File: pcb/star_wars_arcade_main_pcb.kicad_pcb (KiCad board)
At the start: 2 copper layers, 292.1 x 525.8 mm, 322 parts, among them J16 Aud_Conn, J17 Main_Connector, J18 Cat_Box_Conn, J20 J20, Q1 2N3904, Q3 Q_NPN_BCE, Q4 Q_NPN_BCE, SW1 L_11, SW2 D_10, SW3 E/F_10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

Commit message: 661 unconnected signal remain
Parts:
- moved R95 0.64 mm to (65.4, 203.8)
- moved R97 0.64 mm to (69.2, 201.3)
- moved CR2 0.63 mm to (54.6, 170.2)
- moved R91 0.63 mm to (54.0, 154.9)
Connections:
- D_9 pad 12: 3GCLK -> 1.5GCLK
- D_9 pad 13: 1.5GCLK -> 3GCLK
- K_9 pad 14: D6 -> D1
- K_9 pad 15: D5 -> D2
- K_9 pad 17: D7 -> D0
- K_9 pad 18: D3 -> D4
- K_9 pad 19: D2 -> D5
- K_9 pad 20: D1 -> D6
- K_9 pad 21: D0 -> D7
- K_9 pad 8: D4 -> D3
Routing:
- net D1: track 284.5 -> 626.1 mm
- net D2: track 309.2 -> 630.6 mm, vias 6 -> 8
- net ~PRNGCLR: track 57.8 -> 366.0 mm, vias 0 -> 2
- net GND: track 7544.9 -> 7828.7 mm, vias 59 -> 60
- net Net-(C_10-Pad10): track 48.9 -> 229.2 mm, vias 1 -> 4
- net ~OPT0: track 0.00 -> 168.3 mm, vias 0 -> 2
- net D7: track 575.2 -> 729.5 mm
- net Net-(D_8-Pad1): track 7.62 -> 159.4 mm, vias 1 -> 2
- net ~OPT1: track 0.00 -> 144.8 mm, vias 0 -> 2
- net AB0: track 523.2 -> 662.3 mm
- net 750KHZ: track 174.6 -> 301.6 mm, vias 1 -> 2
- net ~IN1: track 0.00 -> 126.4 mm, vias 0 -> 2
- net ~RECALL: track 103.5 -> 224.8 mm
- net AB1: track 567.1 -> 687.7 mm, vias 5 -> 6
- net ~RESET: track 380.2 -> 497.1 mm, vias 5 -> 6
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
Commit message: 557 unconnected signals remain
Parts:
- moved R94 1.27 mm to (127.6, 203.2)
- moved C21 0.64 mm to (39.4, 267.3)
- moved C74 0.64 mm to (39.4, 230.5)
- moved C75 0.63 mm to (108.6, 243.2)
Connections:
- N_8 pad 1: 3MHZ -> ~R~WB
- N_8 pad 2: ~R~WB -> 3MHZ
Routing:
- net ~R~WB: track 0.00 -> 470.8 mm, vias 0 -> 3
- net 12MHZ: track 228.0 -> 595.0 mm, vias 4 -> 5
- net AB7: track 346.1 -> 652.8 mm, vias 2 -> 3
- net Net-(N_8-Pad6): track 10.2 -> 275.6 mm, vias 0 -> 2
- net ~OUTS: track 0.00 -> 250.2 mm, vias 0 -> 1
- net 3MHZ: track 260.4 -> 508.5 mm, vias 2 -> 3
- net ~WE: track 294.0 -> 542.2 mm, vias 3 -> 5
- net ~IRQCLR: track 0.00 -> 235.6 mm
- net ~REN: track 0.00 -> 230.8 mm, vias 0 -> 3
- net Net-(K_2-Pad5): track 17.8 -> 247.3 mm, vias 1 -> 2
- net ~MW0: track 0.00 -> 226.7 mm, vias 0 -> 3
- net DS1: track 0.00 -> 222.2 mm, vias 0 -> 4
- net ~3MHZ*: track 16.1 -> 235.8 mm, vias 1 -> 5
- net P93: track 77.5 -> 286.4 mm, vias 1 -> 5
- net ~MBCON: track 174.6 -> 348.2 mm, vias 1 -> 3
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
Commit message: Added more signal traces
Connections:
- M_6 pad 1: Net-(L_6-Pad6) -> Net-(L_6-Pad3)
- M_6 pad 3: Net-(L_6-Pad3) -> Net-(M_6-Pad3)
- N_6 pad 10: Net-(N_6-Pad10) -> Net-(L_6-Pad6)
- P_6 pad 14: Net-(N_6-Pad10) -> Net-(M_6-Pad3)
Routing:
- net Net-(E_6-Pad11): track 15.5 -> 221.5 mm, vias 1 -> 2
- net ~RESET: track 497.1 -> 696.7 mm, vias 6 -> 8
- net ~6MHZ: track 36.8 -> 210.2 mm
- net Net-(M_7-Pad8): track 0.00 -> 167.8 mm, vias 0 -> 3
- net IP1: track 17.8 -> 173.4 mm, vias 1 -> 2
- net ~MW2: track 0.00 -> 144.1 mm, vias 0 -> 1
- net 3MHZ*: track 161.8 -> 293.5 mm, vias 4 -> 6
- net MDB3: track 61.0 -> 177.2 mm, vias 1 -> 4
- net DD2: track 0.00 -> 112.7 mm, vias 0 -> 2
- net MDB4: track 54.2 -> 153.3 mm, vias 1 -> 3
- net DD7: track 0.00 -> 99.1 mm, vias 0 -> 2
- net MDB5: track 38.1 -> 130.2 mm, vias 0 -> 2
- net MDB0: track 54.6 -> 137.7 mm, vias 0 -> 3
- net DB6: track 21.6 -> 101.0 mm, vias 1 -> 3
- net IP7: track 22.9 -> 96.5 mm
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
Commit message: 241 unconnected signals remain
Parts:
- moved C75 0.64 mm to (108.6, 242.6)
- moved C52 0.64 mm to (39.4, 464.2)
- moved C56 0.64 mm to (39.4, 424.2)
- moved C66 0.64 mm to (39.4, 305.4)
- moved C59 0.63 mm to (40.0, 384.2)
- moved C64 0.63 mm to (189.2, 359.4)
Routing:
- net ~EVMEM: track 149.5 -> 484.6 mm, vias 3 -> 5
- net R~W~B: track 371.7 -> 680.3 mm, vias 5 -> 6
- net ~MBRAM: track 76.5 -> 362.8 mm, vias 2 -> 4
- net DB3: track 70.1 -> 339.5 mm, vias 1 -> 6
- net ~DVSRH: track 139.6 -> 368.5 mm, vias 3 -> 5
- net DB6: track 101.0 -> 329.0 mm, vias 3 -> 6
- net AB0: track 662.3 -> 887.1 mm, vias 9 -> 12
- net ~ENA: track 18.4 -> 239.8 mm, vias 1 -> 3
- net DB5: track 73.0 -> 293.4 mm, vias 1 -> 4
- net Net-(E_6-Pad5): track 12.1 -> 228.2 mm, vias 1 -> 2
- net DB4: track 50.2 -> 259.7 mm, vias 1 -> 3
- net Net-(E_5-Pad2): track 19.0 -> 228.6 mm, vias 1 -> 2
- net ~ENB: track 45.7 -> 251.5 mm, vias 1 -> 2
- net DB7: track 167.0 -> 368.3 mm, vias 2 -> 4
- net DB0: track 127.0 -> 300.0 mm, vias 1 -> 2
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
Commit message: 63 disconnected signals remain
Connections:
- D_4 pad 13: D6 -> DB6
- D_4 pad 14: D4 -> DB4
- D_4 pad 15: D2 -> DB2
- D_4 pad 16: D0 -> DB0
- D_4 pad 4: D1 -> DB1
- D_4 pad 5: D3 -> DB3
- D_4 pad 6: D5 -> DB5
- D_4 pad 7: D7 -> DB7
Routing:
- net 1.5MHZ: track 314.9 -> 628.6 mm, vias 5 -> 8
- net DB7: track 368.3 -> 664.7 mm, vias 4 -> 6
- net DB1: track 160.7 -> 434.9 mm, vias 1 -> 5
- net ~R~WB: track 470.8 -> 714.3 mm, vias 3 -> 5
- net R~W: track 83.8 -> 321.9 mm, vias 1 -> 3
- net ECLKQ: track 139.1 -> 366.7 mm, vias 3 -> 5
- net A15: track 156.8 -> 362.8 mm, vias 0 -> 2
- net P96: track 84.5 -> 273.1 mm
- net Net-(M_3-Pad10): track 0.00 -> 177.8 mm, vias 0 -> 1
- net DB6: track 329.0 -> 501.7 mm, vias 6 -> 7
- net 3MHZ: track 531.4 -> 700.3 mm
- net DB0: track 300.0 -> 467.6 mm
- net DD13: track 31.7 -> 198.0 mm, vias 1 -> 3
- net AB0: track 887.1 -> 1048.6 mm, vias 12 -> 13
- net DB4: track 259.7 -> 419.7 mm, vias 3 -> 5
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
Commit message: Completed the layout!
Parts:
- added R1000: 180, Star_Wars_Vector_PCB:GenericComp, F.Cu at (251.5, 138.4)
- moved TP3MHZ1 0.64 mm to (88.9, 462.9)
- moved TPROM4 0.63 mm to (102.2, 463.6)
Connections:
- J_3 pad 12: Net-(J_3-Pad12) -> P96
- K_3 pad 12: Net-(K_3-Pad12) -> P96
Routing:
- net AB9: track 289.6 -> 502.2 mm, vias 5 -> 6
- net ~ROM4: track 57.8 -> 264.2 mm
- net ~ROM3: track 52.7 -> 252.7 mm, vias 0 -> 1
- net 6MHZ: track 155.2 -> 334.9 mm
- net ~ROM2: track 68.6 -> 233.0 mm, vias 0 -> 1
- net AB10: track 301.6 -> 462.9 mm
- net ~ROM0: track 151.8 -> 306.1 mm, vias 1 -> 3
- net ~NOVRAM: track 0.00 -> 144.1 mm, vias 0 -> 2
- net ~NSTORE: track 196.2 -> 307.6 mm, vias 1 -> 2
- net BIC1: track 0.00 -> 92.7 mm
- net ~EVMEM: track 608.5 -> 699.3 mm
- net Net-(B/C_0-Pad13): track 109.7 -> 198.0 mm
- net AB8: track 362.6 -> 448.9 mm
- net BIC2: track 8.26 -> 83.2 mm
- net BIC0: track 0.00 -> 69.2 mm
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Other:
- board text added: "Designed By Nick Mikstas"

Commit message: Updated readme file
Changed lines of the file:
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@@
     (thickness 1.6)
     (drawings 118)
-    (tracks 10588)
+    (tracks 10589)
     (zones 0)
     (modules 323)
@@
     (visible_elements 7FFFF7FF)
     (pcbplotparams
-      (layerselection 0x010fc_ffffffff)
+      (layerselection 0x010f0_ffffffff)
       (usegerberextensions false)
       (usegerberattributes false)
@@
   (segment (start 122.555 363.22) (end 124.46 363.22) (width 0.381) (layer B.Cu) (net 123))
   (segment (start 124.46 363.22) (end 124.46 359.41) (width 0.381) (layer B.Cu) (net 123))
-  (segment (start 122.555 323.215) (end 123.825 323.215) (width 0.381) (layer B.Cu) (net 123))
-  (segment (start 123.825 323.215) (end 123.825 332.74) (width 0.381) (layer B.Cu) (net 123))
-  (segment (start 123.825 332.74) (end 124.46 332.74) (width 0.381) (layer B.Cu) (net 123))
-  (segment (start 124.46 332.74) (end 124.46 340.995) (width 0.381) (layer B.Cu) (net 123))
-  (segment (start 124.46 340.995) (end 123.825 340.995) (width 0.381) (layer B.Cu) (net 123))
-  (segment (start 123.19 342.265) (end 123.825 342.265) (width 0.381) (layer B.Cu) (net 123))
-  (segment (start 123.825 340.995) (end 123.825 342.265) (width 0.381) (layer B.Cu) (net 123))
-  (segment (start 123.825 342.265) (end 123.825 344.805) (width 0.381) (layer B.Cu) (net 123))
-  (segment (start 124.46 344.805) (end 124.46 359.41) (width 0.381) (layer B.Cu) (net 123))
-  (segment (start 123.825 344.805) (end 124.46 344.805) (width 0.381) (layer B.Cu) (net 123))
   (segment (start 161.29 274.955) (end 163.83 274.955) (width 0.381) (layer B.Cu) (net 123))
   (segment (start 161.29 309.245) (end 161.29 274.955) (width 0.381) (layer B.Cu) (net 123))
@@
   (segment (start 247.015 361.95) (end 247.015 360.68) (width 0.381) (layer F.Cu) (net 123))
   (segment (start 222.885 363.22) (end 222.885 361.95) (width 0.381) (layer F.Cu) (net 123))
+  (segment (start 123.825 344.805) (end 124.46 344.805) (width 0.381) (layer B.Cu) (net 123))
+  (segment (start 123.825 323.215) (end 123.825 332.74) (width 0.381) (layer B.Cu) (net 123))
+  (segment (start 124.46 332.74) (end 124.46 340.995) (width 0.381) (layer B.Cu) (net 123))
+  (segment (start 123.825 332.74) (end 124.46 332.74) (width 0.381) (layer B.Cu) (net 123))
+  (segment (start 124.46 344.805) (end 124.46 359.41) (width 0.381) (layer B.Cu) (net 123))
+  (segment (start 122.555 323.215) (end 123.825 323.215) (width 0.381) (layer B.Cu) (net 123))
+  (segment (start 124.46 340.995) (end 123.825 340.995) (width 0.381) (layer B.Cu) (net 123))
+  (segment (start 123.825 344.805) (end 123.825 342.9) (width 0.381) (layer B.Cu) (net 123))
+  (segment (start 123.825 342.9) (end 123.19 342.265) (width 0.381) (layer B.Cu) (net 123))
+  (segment (start 123.825 340.995) (end 123.825 341.63) (width 0.381) (layer B.Cu) (net 123))
+  (segment (start 123.825 341.63) (end 123.19 342.265) (width 0.381) (layer B.Cu) (net 123))
   (segment (start 241.935 355.6) (end 229.87 355.6) (width 0.381) (layer F.Cu) (net 124))
   (segment (start 229.87 355.6) (end 229.87 355.6) (width 0.381) (layer F.Cu) (net 124))

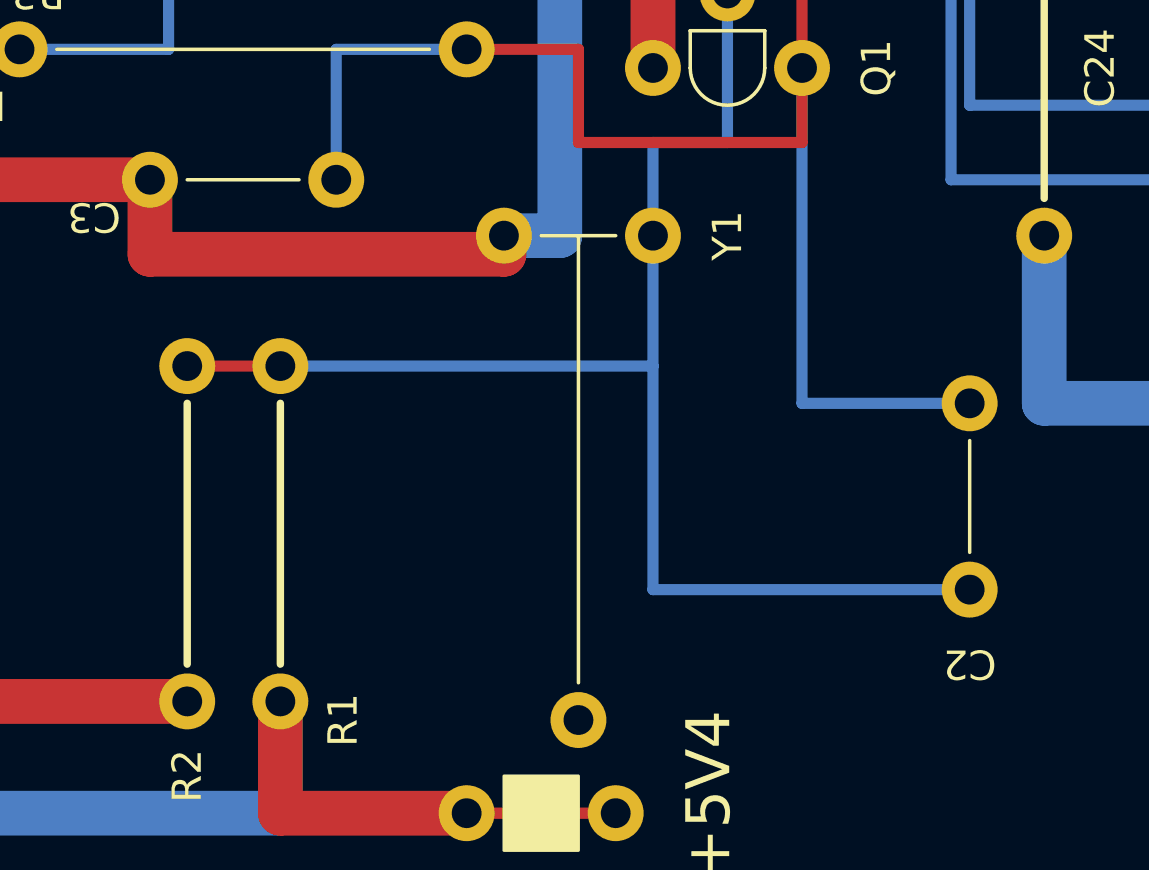
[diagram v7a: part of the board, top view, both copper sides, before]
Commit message: Added BOM and fixed minor silkscreen issues
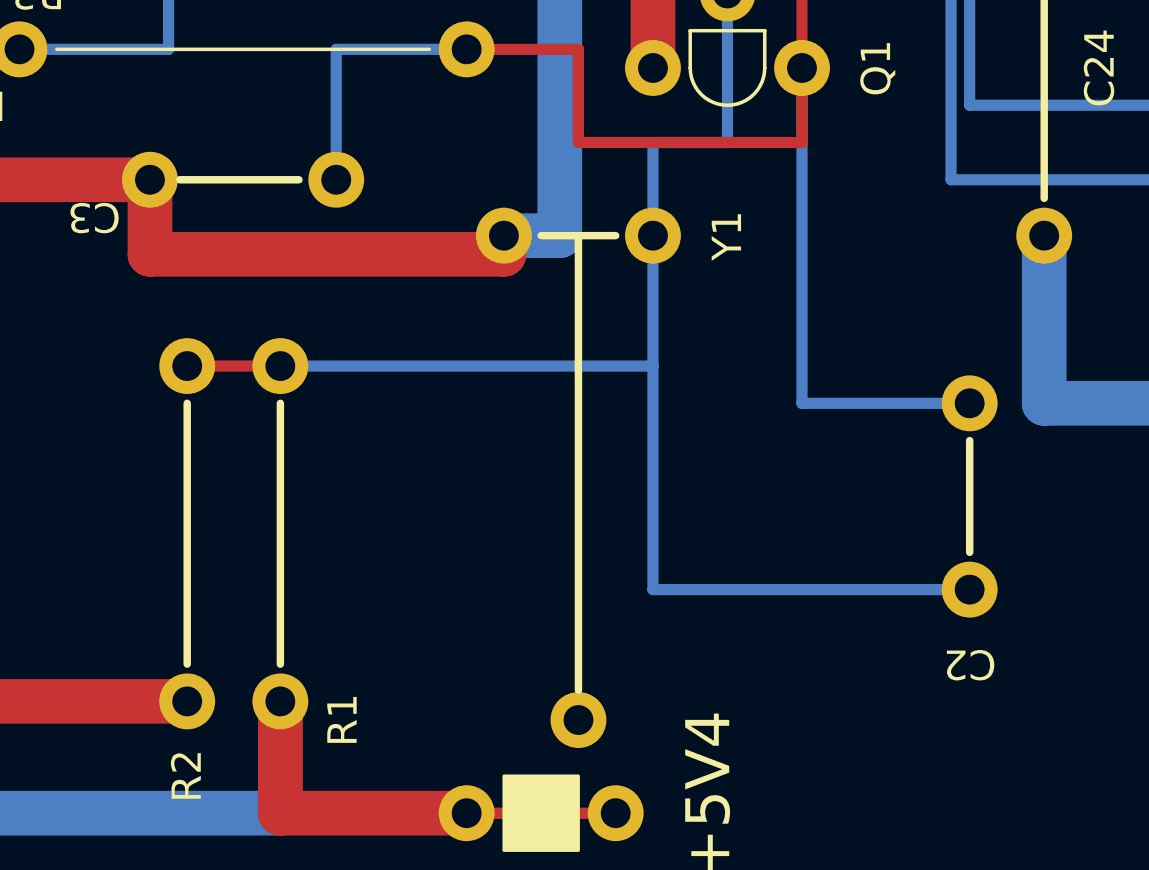
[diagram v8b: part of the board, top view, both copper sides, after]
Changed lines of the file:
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@@
   (general
     (thickness 1.6)
-    (drawings 118)
+    (drawings 122)
     (tracks 10589)
     (zones 0)
@@
   )
   (setup
-    (last_trace_width 0.381)
+    (last_trace_width 0.25)
     (user_trace_width 0.381)
     (user_trace_width 0.762)
@@
       (net 2 GND))
   )
+  (gr_line (start 54.61 480.695) (end 52.07 480.695) (layer F.SilkS) (width 0.254))
+  (gr_line (start 53.34 480.695) (end 53.34 496.189) (layer F.SilkS) (width 0.254))
+  (gr_line (start 39.751 478.79) (end 43.815 478.79) (layer F.SilkS) (width 0.254))
+  (gr_line (start 66.675 491.49) (end 66.675 487.68) (layer F.SilkS) (width 0.254))
   (gr_text "Designed By Nick Mikstas" (at 313.69 518.16 90) (layer F.SilkS)
     (effects (font (size 1.524 1.524) (thickness 0.3048)))
@@
   (gr_line (start 247.015 537.21) (end 227.33 537.21) (angle 90) (layer Edge.Cuts) (width 0.0254))
   (gr_arc (start 113.03 538.48) (end 113.03 537.21) (angle 90) (layer Edge.Cuts) (width 0.0254))
-  (via (at 110.49 398.78) (size 1.524) (drill 1.016) (layers F.Cu B.Cu) (net 9))
-  (via (at 212.725 356.87) (size 1.524) (drill 1.016) (layers F.Cu B.Cu) (net 64))
   (via (at 189.23 346.71) (size 1.524) (drill 1.016) (layers F.Cu B.Cu) (net 1))
   (via (at 108.585 346.71) (size 1.524) (drill 1.016) (layers F.Cu B.Cu) (net 1))
@@
   (segment (start 285.75 521.97) (end 285.115 521.335) (width 0.381) (layer B.Cu) (net 8))
   (segment (start 283.845 502.285) (end 281.305 502.285) (width 0.381) (layer B.Cu) (net 8))
+  (via (at 110.49 398.78) (size 1.524) (drill 1.016) (layers F.Cu B.Cu) (net 9))
   (segment (start 198.12 541.02) (end 198.12 534.035) (width 0.381) (layer F.Cu) (net 9))
   (segment (start 198.12 534.035) (end 198.12 534.035) (width 0.381) (layer F.Cu) (net 9))
@@
   (segment (start 278.13 447.675) (end 280.67 447.675) (width 0.381) (layer B.Cu) (net 63))
   (segment (start 280.67 447.675) (end 280.67 444.5) (width 0.381) (layer B.Cu) (net 63))
+  (via (at 212.725 356.87) (size 1.524) (drill 1.016) (layers F.Cu B.Cu) (net 64))
   (via (at 202.565 512.445) (size 1.524) (drill 1.016) (layers F.Cu B.Cu) (net 64))
   (segment (start 270.51 429.26) (end 270.51 425.45) (width 0.381) (layer B.Cu) (net 64))
